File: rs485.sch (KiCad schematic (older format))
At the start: 4 parts, among them J5 Conn_01x02, U4 SP3481CN

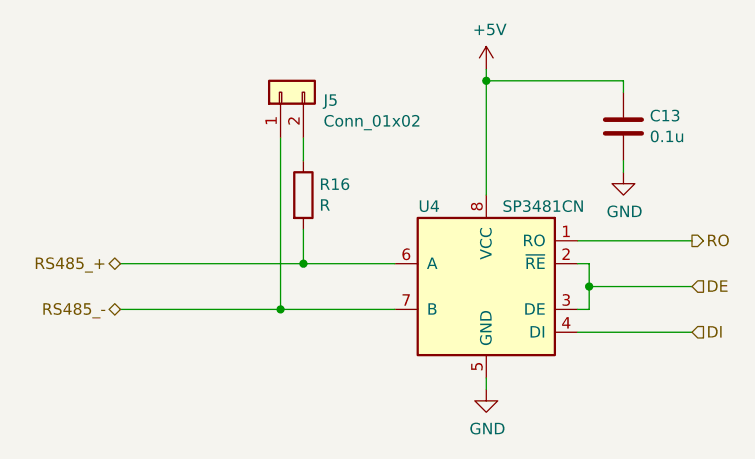
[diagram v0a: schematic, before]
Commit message: 見つけた設計ミスを全部反映
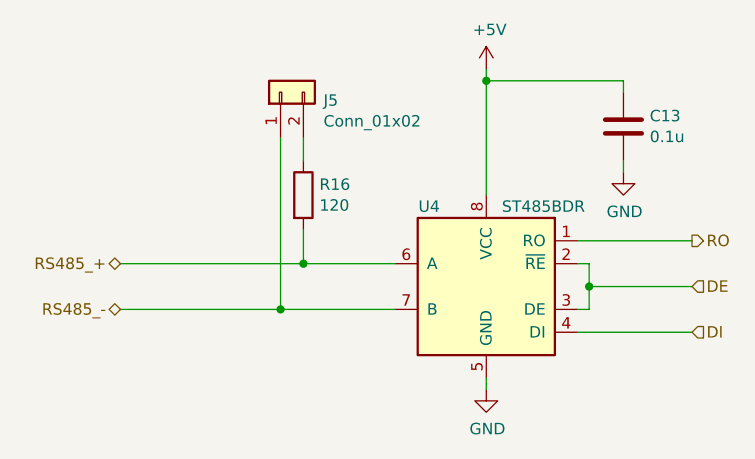
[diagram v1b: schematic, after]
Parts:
- removed U4: SP3481CN, Package_SO:SOIC-8_3.9x4.9mm_P1.27mm, symbol Interface_UART:SP3481CN
- added U4: ST485BDR, Package_SO:SOIC-8_3.9x4.9mm_P1.27mm, symbol mylib:ST485BDR
- R16: value R -> 120
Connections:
- net +5V: now also U4.8 (VCC)
- net DE: now also U4.2 (~RE~), U4.3 (DE)
- net DI: now also U4.4 (DI)
- net GND: now also U4.5 (GND)
- net RO: now also U4.1 (RO)
- net RS485_+: now also U4.6 (A)
- net RS485_-: now also U4.7 (B)
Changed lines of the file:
@@
 EESchema Schematic File Version 4
-LIBS:Encoder_check-cache
 EELAYER 30 0
 EELAYER END
@@
 Comment4 ""
 $EndDescr
-$Comp
-L Interface_UART:SP3481CN U4
-U 1 1 5E328515
-P 5850 4100
-F 0 "U4" H 6100 4450 50  0000 C CNN
-F 1 "SP3481CN" H 5600 4450 50  0000 C CNN
-F 2 "Package_SO:SOIC-8_3.9x4.9mm_P1.27mm" H 6900 3750 50  0001 C CIN
-F 3 "http://www.icbase.com/pdf/SPX/SPX00480106.pdf" H 5850 4100 50  0001 C CNN
-	1    5850 4100
-	-1   0    0    -1
-$EndComp
 $Comp
 L power:GND #PWR0140
@@
 P 5050 3700
 F 0 "R16" H 5120 3746 50  0000 L CNN
-F 1 "R" H 5120 3655 50  0000 L CNN
+F 1 "120" H 5120 3655 50  0000 L CNN
 F 2 "Resistor_SMD:R_0603_1608Metric" V 4980 3700 50  0001 C CNN
 F 3 "~" H 5050 3700 50  0001 C CNN
@@
 Wire Wire Line
 	4950 4200 5450 4200
+$Comp
+L mylib:ST485BDR U4
+U 1 1 5E65BC93
+P 5850 4100
+F 0 "U4" H 6100 4450 50  0000 C CNN
+F 1 "ST485BDR" H 5600 4450 50  0000 C CNN
+F 2 "Package_SO:SOIC-8_3.9x4.9mm_P1.27mm" H 6900 3750 50  0001 C CIN
+F 3 "https://www.st.com/resource/en/datasheet/st485b.pdf" H 5850 4100 50  0001 C CNN
+	1    5850 4100
+	-1   0    0    -1
+$EndComp
 $EndSCHEMATC
